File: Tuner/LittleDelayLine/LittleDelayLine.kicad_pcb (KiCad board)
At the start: 2 copper layers, 100 x 100 mm, 116 parts, among them J1 Conn_Coaxial, J10 Conn_Coaxial, J11 Conn_02x05_Odd_Even, J12 Conn_01x01, J13 Conn_01x01, J14 Conn_01x01, J15 Conn_01x01, J16 Conn_01x01, J17 Conn_Coaxial, J18 Conn_01x01, J19 Conn_01x01, J2 Conn_Coaxial, J20 Conn_01x01, J21 Conn_01x01, J22 Conn_Coaxial, J23 Conn_Coaxial, J24 Conn_Coaxial, J25 Conn_01x01, J26 Conn_01x01, J27 Conn_01x01, J28 Conn_01x01, J3 Conn_Coaxial, J4 Conn_Coaxial, J5 Conn_Coaxial, J6 Conn_Coaxial, J7 Conn_Coaxial, J8 Conn_Coaxial, J9 Conn_Coaxial, P10 Conn_01x01, P11 Conn_01x01, P12 Conn_01x01, P2 Conn_01x01, P3 Conn_01x01, P4 Conn_01x01, P5 Conn_01x01, P6 Conn_01x01, P7 Conn_01x01, P8 Conn_01x01, P9 Conn_01x01, U1 MCP23008, U2 ULN2803A

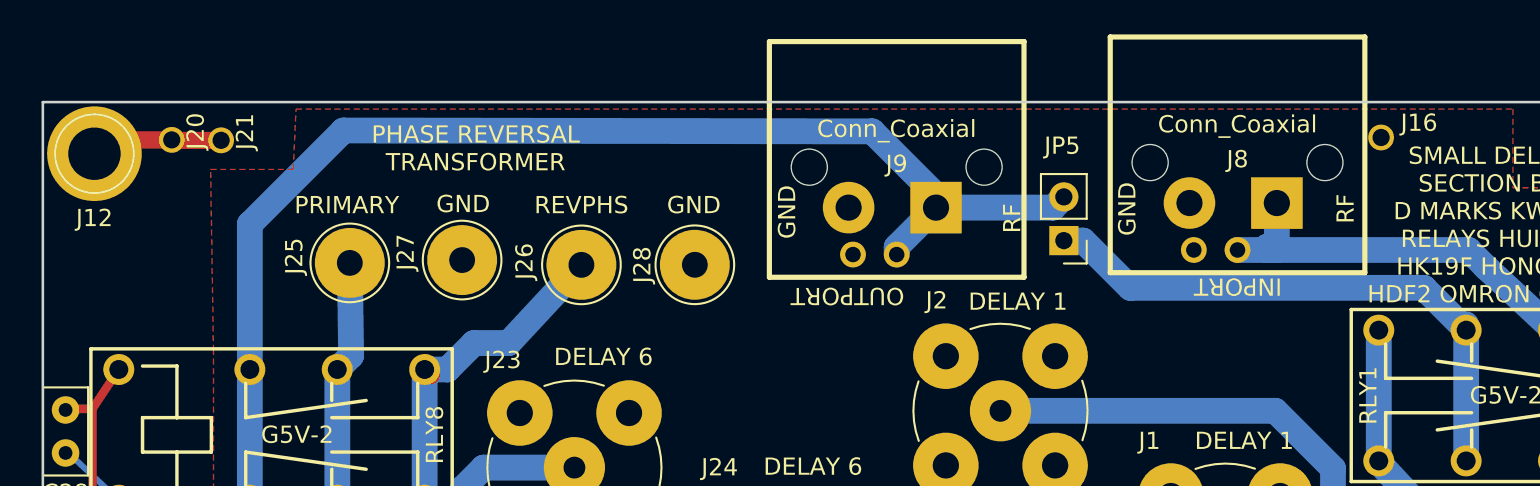
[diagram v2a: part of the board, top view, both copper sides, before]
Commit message: TandenMatch now has DC-RF bias tee
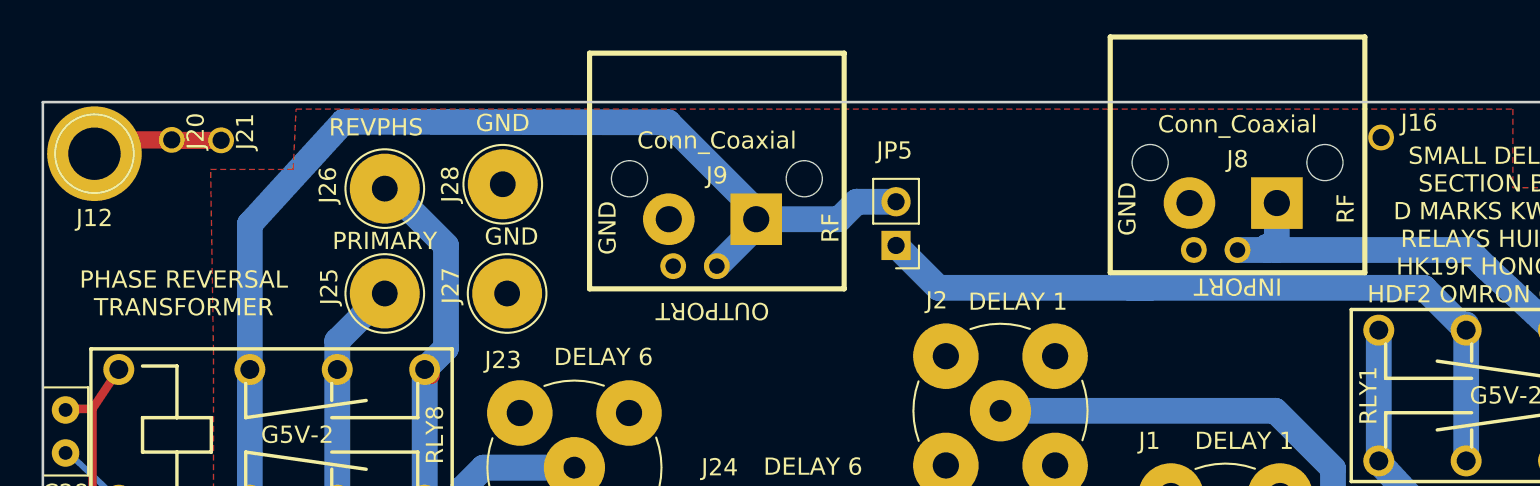
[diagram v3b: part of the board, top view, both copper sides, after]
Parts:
- moved J26 12.3 mm to (69.9, 55.0)
- moved J28 12.1 mm to (76.7, 54.8)
- moved J9 10.5 mm to (89.2, 47.2)
- moved JP5 9.76 mm to (99.6, 58.3)
- moved J27 3.26 mm to (77.0, 61.1)
- moved J25 2.70 mm to (69.9, 61.1)
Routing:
- net Net-(JP5-Pad1): track 33.5 -> 44.2 mm
- net RFOUT: track 72.6 -> 64.5 mm
- net Net-(J25-Pad1): track 21.7 -> 20.7 mm
- net Net-(J26-Pad1): track 19.5 -> 20.4 mm
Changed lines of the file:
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@@
     (thickness 1.6)
     (drawings 41)
-    (tracks 738)
+    (tracks 741)
     (zones 0)
     (modules 116)
@@
   )
   (module Connectors:1pin (layer F.Cu)
-    (at 67.8434 59.3471)
+    (at 69.8754 61.1251)
     (descr "module 1 pin (ou trou mecanique de percage)")
     (tags DEV)
@@
   )
   (module Connectors:1pin (layer F.Cu)
-    (at 81.3054 59.4614)
+    (at 69.8754 55.0291)
     (descr "module 1 pin (ou trou mecanique de percage)")
     (tags DEV)
@@
   )
   (module Connectors:1pin (layer F.Cu)
-    (at 74.3712 59.182)
+    (at 76.9874 61.1251)
     (descr "module 1 pin (ou trou mecanique de percage)")
     (tags DEV)
@@
   )
   (module Connectors:1pin (layer F.Cu)
-    (at 87.89924 59.45632 90)
+    (at 76.7334 54.7751 90)
     (descr "module 1 pin (ou trou mecanique de percage)")
     (tags DEV)
@@
   )
   (module tuner:bnc_90_1-1337543-0_pad_combo (layer F.Cu)
-    (at 99.6315 46.482 180)
+    (at 89.1794 47.1551 180)
     (descr "BNC connector, Tyco 1-1337543-0")
     (fp_text reference J9 (at 0 -7.112 180) (layer F.SilkS)
@@
   )
   (module Pin_Headers:Pin_Header_Straight_1x02_Pitch2.54mm (layer F.Cu)
-    (at 109.347 58.0517 180)
+    (at 99.5934 58.3311 180)
     (descr "Through hole straight pin header, 1x02, 2.54mm pitch, single row")
     (tags "Through hole pin header THT 1x02 2.54mm single row")
@@
     )
   )
-  (gr_text GND (at 87.84336 55.99176) (layer F.SilkS)
+  (gr_text GND (at 77.2414 57.8231) (layer F.SilkS)
     (effects (font (size 1 1) (thickness 0.15)))
   )
-  (gr_text OUTPORT (at 96.774 61.2648 180) (layer F.SilkS)
+  (gr_text OUTPORT (at 88.9254 62.1411 180) (layer F.SilkS)
     (effects (font (size 1 1) (thickness 0.15)))
   )
-  (gr_text "PHASE REVERSAL\nTRANSFORMER" (at 75.1586 52.69484) (layer F.SilkS)
+  (gr_text "PHASE REVERSAL\nTRANSFORMER" (at 58.1914 61.1251) (layer F.SilkS)
     (effects (font (size 1 1) (thickness 0.15)))
   )
@@
     (effects (font (size 1 1) (thickness 0.15)))
   )
-  (gr_text PRIMARY (at 67.6656 55.9943) (layer F.SilkS)
+  (gr_text PRIMARY (at 69.8754 58.0771) (layer F.SilkS)
     (effects (font (size 1 1) (thickness 0.15)))
   )
-  (gr_text REVPHS (at 81.3054 55.9943) (layer F.SilkS)
+  (gr_text REVPHS (at 69.3674 51.4731) (layer F.SilkS)
     (effects (font (size 1 1) (thickness 0.15)))
   )
-  (gr_text GND (at 74.4347 55.9308) (layer F.SilkS)
+  (gr_text GND (at 76.7334 51.2191) (layer F.SilkS)
     (effects (font (size 1 1) (thickness 0.15)))
   )
-  (gr_text RF (at 106.3498 56.7563 90) (layer F.SilkS)
+  (gr_text RF (at 95.7834 57.3151 90) (layer F.SilkS)
     (effects (font (size 1 1) (thickness 0.15)))
   )
-  (gr_text GND (at 93.2688 56.388 90) (layer F.SilkS)
+  (gr_text GND (at 82.8294 57.3151 90) (layer F.SilkS)
     (effects (font (size 1 1) (thickness 0.15)))
   )
@@
   (segment (start 75.819 92.9894) (end 86.1695 92.9894) (width 1.5) (layer B.Cu) (net 57))
   (segment (start 72.4357 96.3727) (end 75.819 92.9894) (width 1.5) (layer B.Cu) (net 57))
-  (segment (start 101.9175 56.134) (end 101.9175 55.4101) (width 1.5) (layer B.Cu) (net 58))
-  (segment (start 101.9175 55.4101) (end 98.2091 51.7017) (width 1.5) (layer B.Cu) (net 58))
-  (segment (start 101.9175 56.134) (end 108.7247 56.134) (width 1.5) (layer B.Cu) (net 58))
-  (segment (start 108.7247 56.134) (end 109.347 55.5117) (width 1.5) (layer B.Cu) (net 58))
-  (segment (start 99.6315 58.862) (end 99.6315 58.42) (width 1.5) (layer B.Cu) (net 58) (status 30))
-  (segment (start 99.6315 58.42) (end 101.9175 56.134) (width 1.5) (layer B.Cu) (net 58) (status 30))
-  (segment (start 101.3587 55.5752) (end 101.9175 56.134) (width 1.5) (layer B.Cu) (net 58) (status 30))
+  (segment (start 91.4654 56.8071) (end 91.4654 57.2491) (width 1.5) (layer B.Cu) (net 58))
+  (segment (start 91.4654 57.2491) (end 89.1794 59.5351) (width 1.5) (layer B.Cu) (net 58))
+  (segment (start 91.4654 56.8071) (end 96.2914 56.8071) (width 1.5) (layer B.Cu) (net 58))
+  (segment (start 97.3074 55.7911) (end 99.5934 55.7911) (width 1.5) (layer B.Cu) (net 58))
+  (segment (start 96.2914 56.8071) (end 97.3074 55.7911) (width 1.5) (layer B.Cu) (net 58))
+  (segment (start 91.4654 56.8071) (end 91.4654 56.2991) (width 1.5) (layer B.Cu) (net 58))
+  (segment (start 91.4654 56.2991) (end 86.340382 51.174082) (width 1.5) (layer B.Cu) (net 58))
+  (segment (start 91.4654 56.8071) (end 91.4654 56.0832) (width 1.5) (layer B.Cu) (net 58) (status 30))
+  (segment (start 90.9066 56.2483) (end 91.4654 56.8071) (width 1.5) (layer B.Cu) (net 58) (status 30))
   (segment (start 62.0344 65.542) (end 62.0344 57.0916) (width 1.5) (layer B.Cu) (net 58))
-  (segment (start 67.4751 51.6509) (end 98.2091 51.7017) (width 1.5) (layer B.Cu) (net 58))
-  (segment (start 62.0344 57.0916) (end 67.4751 51.6509) (width 1.5) (layer B.Cu) (net 58))
+  (segment (start 67.4751 51.1429) (end 86.340382 51.174082) (width 1.5) (layer B.Cu) (net 58))
+  (segment (start 62.0344 57.0916) (end 67.4751 51.1429) (width 1.5) (layer B.Cu) (net 58))
   (segment (start 62.0344 73.142) (end 62.0344 65.542) (width 1.5) (layer B.Cu) (net 58))
   (segment (start 72.4357 91.3738) (end 72.4357 89.502) (width 1.5) (layer B.Cu) (net 59))
@@
   (segment (start 74.7141 81.915) (end 74.7141 79.8576) (width 1.5) (layer B.Cu) (net 61))
   (segment (start 72.3214 84.3077) (end 74.7141 81.915) (width 1.5) (layer B.Cu) (net 61))
-  (segment (start 67.8434 59.3471) (end 67.9196 64.7368) (width 1.5) (layer B.Cu) (net 62) (status 10))
-  (segment (start 67.9196 64.7368) (end 67.1144 65.542) (width 1.5) (layer B.Cu) (net 62))
+  (segment (start 67.1144 65.542) (end 67.1144 63.8861) (width 1.5) (layer B.Cu) (net 62))
+  (segment (start 67.1144 63.8861) (end 69.8754 61.1251) (width 1.5) (layer B.Cu) (net 62))
   (segment (start 67.1144 73.142) (end 67.1144 73.5811) (width 1.5) (layer B.Cu) (net 62))
   (segment (start 67.1144 73.5811) (end 62.1614 78.5341) (width 1.5) (layer B.Cu) (net 62))
   (segment (start 67.1144 65.542) (end 67.1144 73.142) (width 1.5) (layer B.Cu) (net 62))
   (segment (start 67.4954 73.4976) (end 67.5794 73.4976) (width 1) (layer F.Cu) (net 62) (status 30))
-  (segment (start 72.1944 65.542) (end 73.523 65.542) (width 1.5) (layer B.Cu) (net 63))
-  (segment (start 77.0763 64.008) (end 81.3054 59.4614) (width 1.5) (layer B.Cu) (net 63) (status 20))
-  (segment (start 75.057 64.008) (end 77.0763 64.008) (width 1.5) (layer B.Cu) (net 63))
-  (segment (start 73.523 65.542) (end 75.057 64.008) (width 1.5) (layer B.Cu) (net 63))
+  (segment (start 69.8754 55.0291) (end 70.1294 55.0291) (width 1.5) (layer B.Cu) (net 63))
+  (segment (start 70.1294 55.0291) (end 73.4314 58.3311) (width 1.5) (layer B.Cu) (net 63))
+  (segment (start 73.4314 58.3311) (end 73.4314 64.305) (width 1.5) (layer B.Cu) (net 63))
+  (segment (start 73.4314 64.305) (end 72.1944 65.542) (width 1.5) (layer B.Cu) (net 63))
   (segment (start 72.1944 65.542) (end 72.1944 73.142) (width 1.5) (layer B.Cu) (net 63))
   (segment (start 72.5754 65.8976) (end 72.5754 65.7657) (width 1) (layer F.Cu) (net 63) (status 30))
@@
   (segment (start 137.8128 63.256) (end 137.8128 70.856) (width 1.5) (layer B.Cu) (net 76) (status 30))
   (segment (start 133.896312 59.613572) (end 137.8128 63.256) (width 1.5) (layer B.Cu) (net 76) (status 20))
-  (segment (start 109.347 58.0517) (end 110.46714 58.0517) (width 1.5) (layer B.Cu) (net 77))
+  (segment (start 114.3254 60.79744) (end 102.05974 60.79744) (width 1.5) (layer B.Cu) (net 77))
+  (segment (start 102.05974 60.79744) (end 99.5934 58.3311) (width 1.5) (layer B.Cu) (net 77))
   (segment (start 130.27424 60.79744) (end 132.7328 63.256) (width 1.5) (layer B.Cu) (net 77))
-  (segment (start 113.21288 60.79744) (end 130.27424 60.79744) (width 1.5) (layer B.Cu) (net 77))
-  (segment (start 110.46714 58.0517) (end 113.21288 60.79744) (width 1.5) (layer B.Cu) (net 77))
+  (segment (start 113.21288 60.79744) (end 114.3254 60.79744) (width 1.5) (layer B.Cu) (net 77))
+  (segment (start 114.3254 60.79744) (end 130.27424 60.79744) (width 1.5) (layer B.Cu) (net 77))
   (segment (start 132.7328 63.256) (end 132.7328 62.9209) (width 1.5) (layer B.Cu) (net 77) (status 30))
   (segment (start 132.7328 63.256) (end 132.7328 70.856) (width 1.5) (layer B.Cu) (net 77) (status 30))

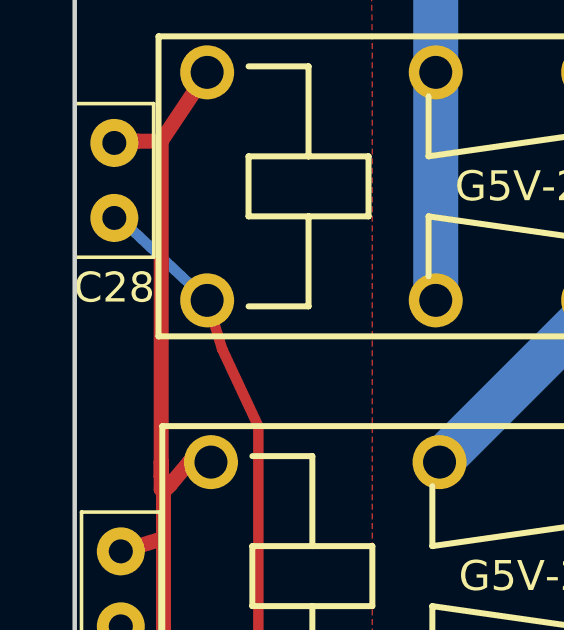
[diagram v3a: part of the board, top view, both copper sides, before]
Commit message: Symmetrized QuadCoupler Layout
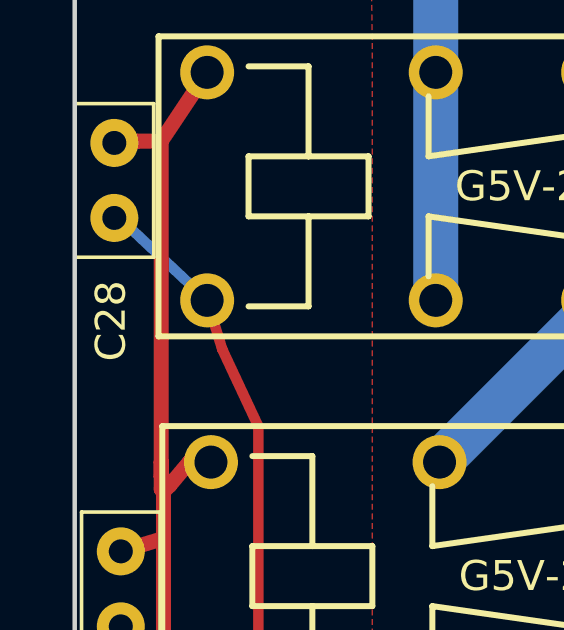
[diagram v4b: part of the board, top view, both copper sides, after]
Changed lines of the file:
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@@
   )
   (setup
-    (last_trace_width 1.5)
+    (last_trace_width 0.25)
     (user_trace_width 0.35)
     (user_trace_width 0.5)
@@
     (descr "C, Disc series, Radial, pin pitch=2.50mm, , diameter*width=5*2.5mm^2, Capacitor, http://cdn-reichelt.de/documents/datenblatt/B300/DS_KERKO_TC.pdf")
     (tags "C Disc series Radial pin pitch 2.50mm  diameter 5mm width 2.5mm Capacitor")
-    (fp_text reference C28 (at 4.826 0 360) (layer F.SilkS)
-      (effects (font (size 1 1) (thickness 0.15)))
-    )
+    (fp_text reference C28 (at 5.9309 0.1143 450) (layer F.SilkS)
+      (effects (font (size 1 1) (thickness 0.15)))
+    )

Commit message: A few tweaks
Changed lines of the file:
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@@
     (links 261)
     (no_connects 0)
-    (area 49.924999 49.924999 150.075001 150.075001)
+    (area 44.281218 45.7653 152.3901 153.921938)
     (thickness 1.6)
     (drawings 41)
-    (tracks 741)
+    (tracks 743)
     (zones 0)
     (modules 116)
@@
   )
   (setup
-    (last_trace_width 0.25)
+    (last_trace_width 1.5)
     (user_trace_width 0.35)
     (user_trace_width 0.5)
@@
   (segment (start 74.4093 72.4535) (end 75.6158 71.247) (width 1.5) (layer B.Cu) (net 60))
   (segment (start 75.6158 71.247) (end 80.899 71.247) (width 1.5) (layer B.Cu) (net 60))
+  (segment (start 75.85075 78.72095) (end 86.37905 78.72095) (width 1.5) (layer B.Cu) (net 61))
+  (segment (start 86.37905 78.72095) (end 87.503 77.597) (width 1.5) (layer B.Cu) (net 61))
   (segment (start 72.3214 86.1341) (end 72.3214 84.3077) (width 1.5) (layer B.Cu) (net 61))
-  (segment (start 76.9747 77.597) (end 93.345 77.597) (width 1.5) (layer B.Cu) (net 61))
-  (segment (start 74.7141 79.8576) (end 76.9747 77.597) (width 1.5) (layer B.Cu) (net 61))
+  (segment (start 87.503 77.597) (end 93.345 77.597) (width 1.5) (layer B.Cu) (net 61))
+  (segment (start 74.7141 79.8576) (end 75.85075 78.72095) (width 1.5) (layer B.Cu) (net 61))
   (segment (start 74.7141 81.915) (end 74.7141 79.8576) (width 1.5) (layer B.Cu) (net 61))
   (segment (start 72.3214 84.3077) (end 74.7141 81.915) (width 1.5) (layer B.Cu) (net 61))

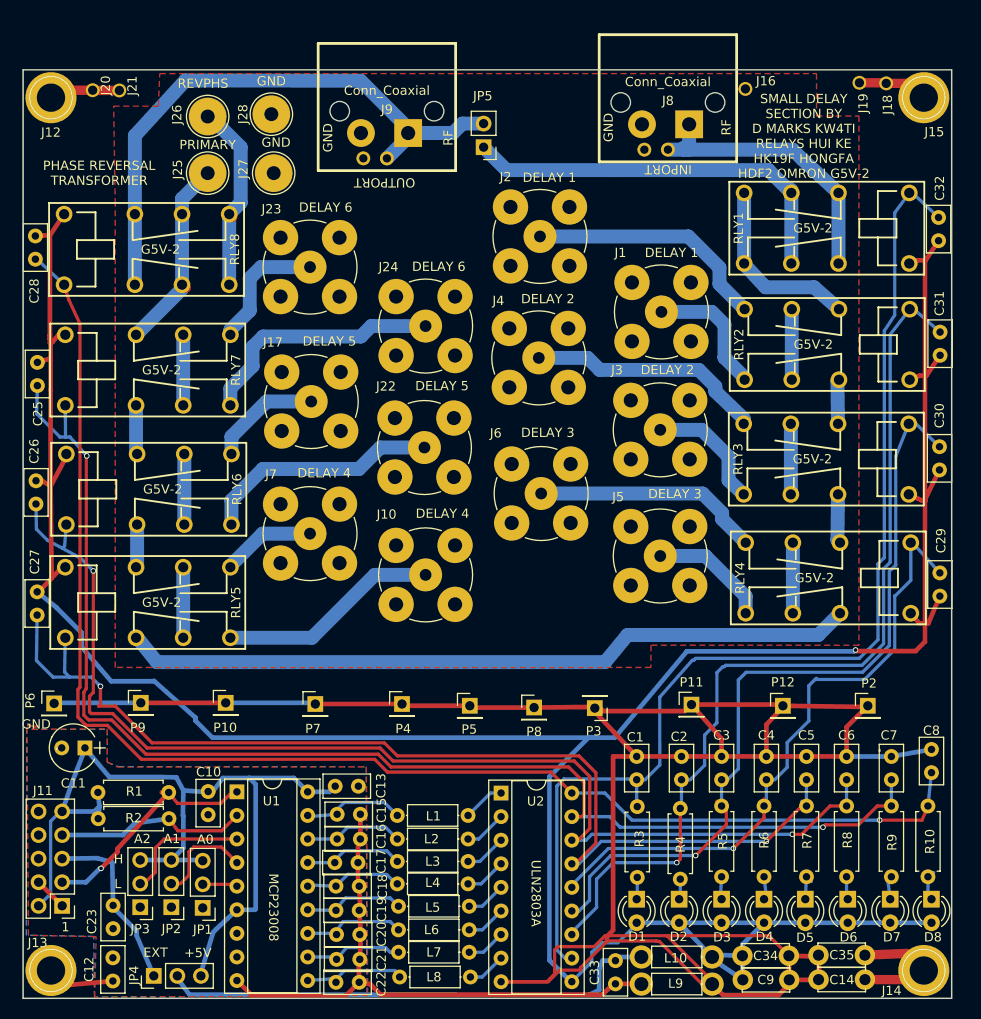
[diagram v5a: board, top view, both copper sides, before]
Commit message: Changed bypass method on delay lines
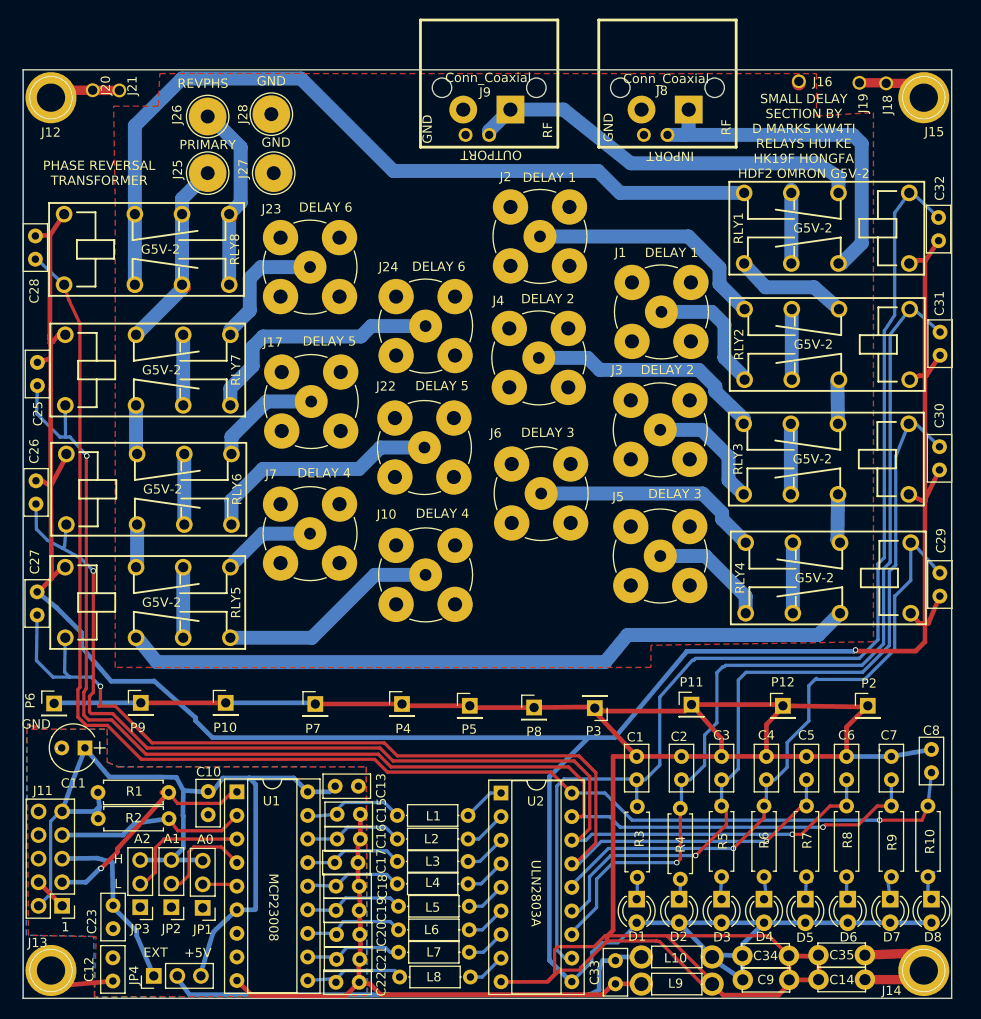
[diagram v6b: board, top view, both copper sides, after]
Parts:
- removed JP5: Jumper_NC_Small, Pin_Headers:Pin_Header_Straight_1x02_Pitch2.54mm
- moved J9 11.3 mm to (100.2, 44.6)
- moved J16 5.81 mm to (134.8, 51.2)
- moved J8 1.59 mm to (119.4, 44.6)
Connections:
- RLY1 pad 6: Net-(J8-Pad1) -> RFOUT
- RLY1 pad 8: Net-(RLY1-Pad4) -> RFTHRU
- RLY8 pad 2: RFOUT -> RFTHRU
- RLY8 pad 6: RFOUT -> RFTHRU
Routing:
- net RFTHRU: track 0.00 -> 89.9 mm
- net Net-(RLY1-Pad3): track 44.2 -> 7.94 mm
- net RFOUT: track 64.5 -> 43.4 mm
- net Net-(RLY1-Pad4): track 19.9 -> 12.3 mm
- net Net-(J8-Pad1): track 31.4 -> 38.6 mm
